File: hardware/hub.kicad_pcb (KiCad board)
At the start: 4 copper layers, 100 x 85 mm, 153 parts, among them J101 USB-A, J102 TNG-Power-BTM, J103 TNG-Power-TOP, J104 TNG-Data-BTM, J105 TNG-Data-TOP, P101 Debug, P102 PE, P202 PWR IN, SW101 BOOT, T201 744272251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

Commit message: fix resistor value, put usb tht connectors in paste layer
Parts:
- R208: value 27 -> 27k
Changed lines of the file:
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@@
     (mod_text_size 1 1)
     (mod_text_width 0.15)
-    (pad_size 1.1 3.8)
-    (pad_drill 0)
+    (pad_size 3.5 3.5)
+    (pad_drill 2.3)
     (pad_to_mask_clearance 0)
     (aux_axis_origin 57.45 50.95)
@@
       (effects (font (size 0.2 0.2) (thickness 0.05)))
     )
-    (fp_text value 27 (at 0.05 -0.375 180) (layer F.Fab)
+    (fp_text value 27k (at 0.05 -0.375 180) (layer F.Fab)
       (effects (font (size 0.2 0.2) (thickness 0.05)))
     )
@@
     (pad 4 smd rect (at 3.5 -4.2 270) (size 1.1 4) (layers F.Cu F.Paste F.Mask)
       (net 67 GND))
-    (pad "" thru_hole circle (at -6.57 0 270) (size 3.5 3.5) (drill 2.3) (layers *.Cu *.Mask))
-    (pad SHD thru_hole circle (at 6.57 0 270) (size 3.5 3.5) (drill 2.3) (layers *.Cu *.Mask F.SilkS)
+    (pad "" thru_hole circle (at -6.57 0 270) (size 3.5 3.5) (drill 2.3) (layers *.Cu *.Mask F.Paste))
+    (pad SHD thru_hole circle (at 6.57 0 270) (size 3.5 3.5) (drill 2.3) (layers *.Cu *.Mask F.Paste)
       (net 1 Earth))
     (model Connectors/USB_Type_B_Socket.wrl

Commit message: fix value
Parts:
- R114: value 510 -> 1k

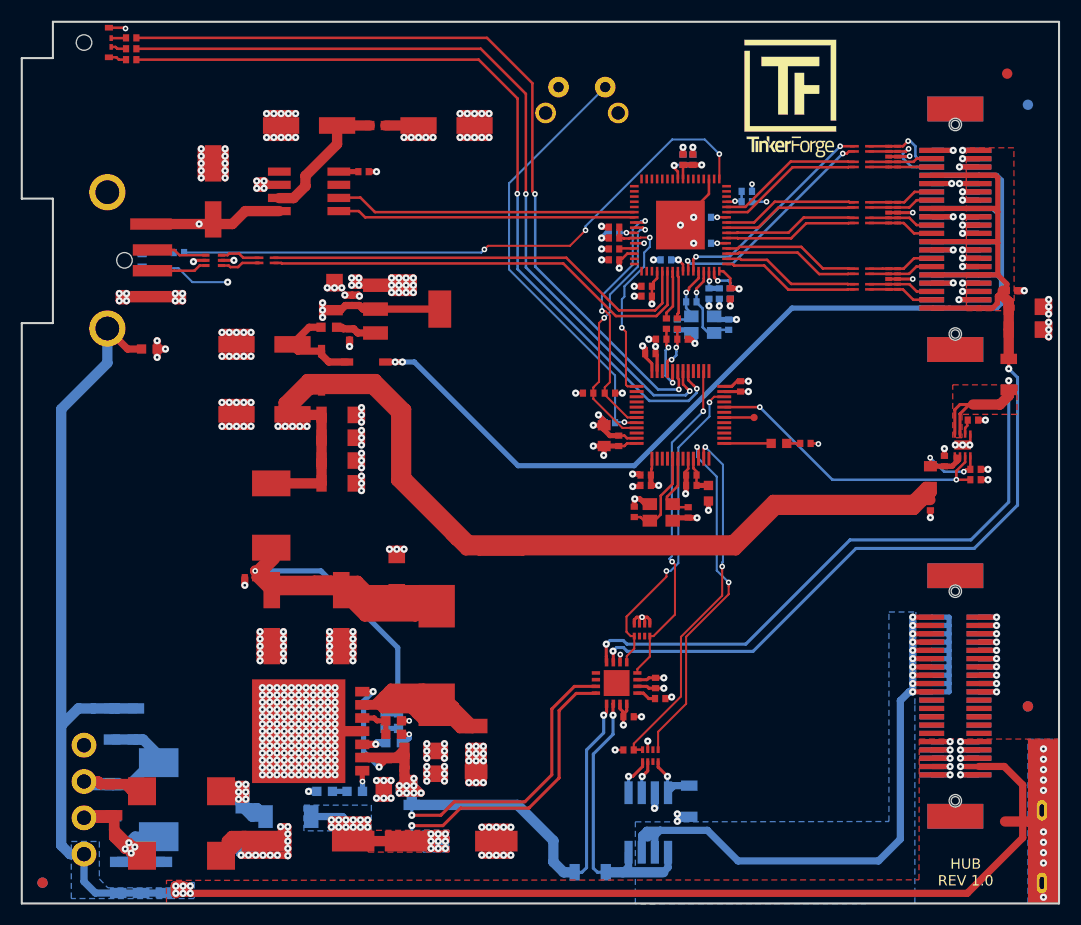
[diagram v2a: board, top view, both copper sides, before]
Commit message: add version 1.2
 * fix footprints
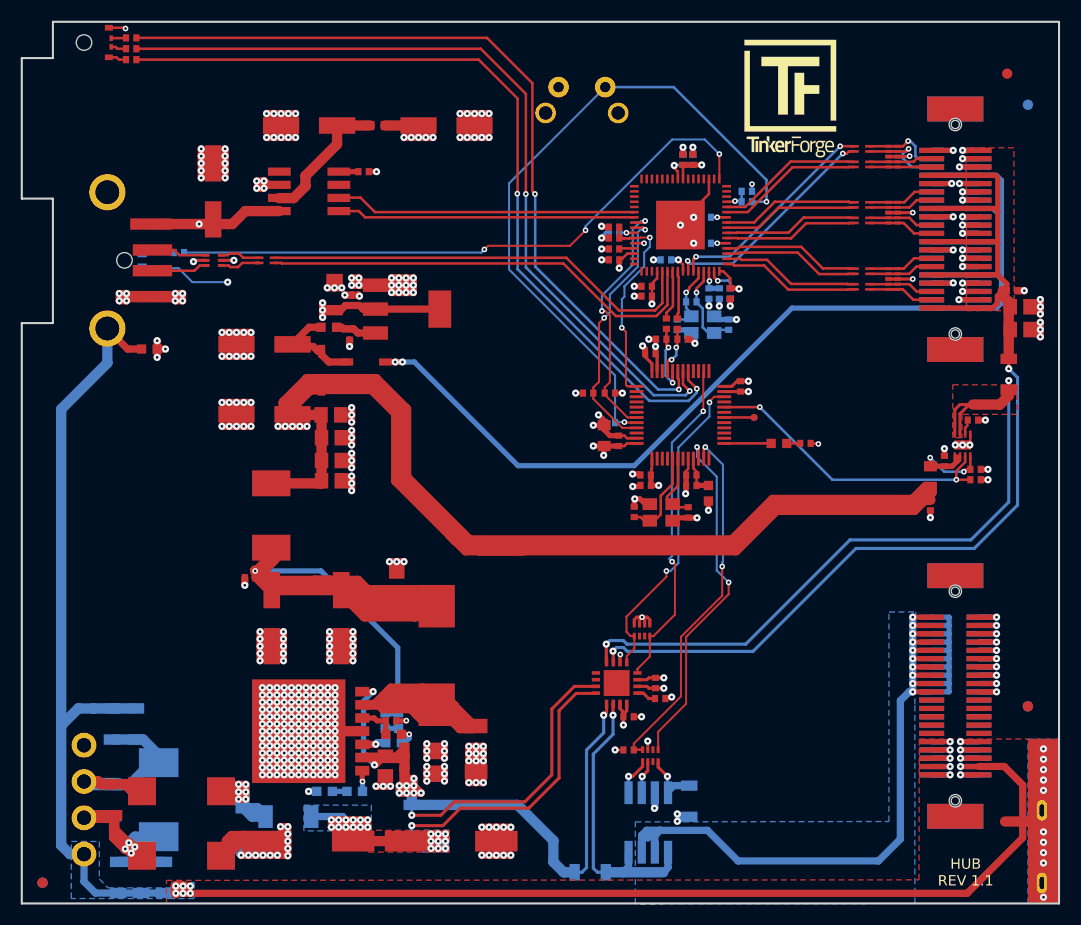
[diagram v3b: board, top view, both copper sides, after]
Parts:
- C108, C109, C117: value >100uF -> 100uF
- C135, C136, C215, C218, C223, C224, C225: footprint C1206 -> kicad-libraries:C0805E
- C137, C138: value TBD -> 12pF
- C201, C202: value 10uF -> 10uF/35V
- C205: value 100nF -> 100nF/35V; footprint C1206 -> kicad-libraries:C0805E
- C208: footprint C0603F -> kicad-libraries:C0402F
- C216, C219, C220: value >100µF -> 100µF
- R108: value 10k -> 1k
- R109: value DNP -> 10k
- T201: footprint kicad-libraries:WE-SL5 -> WE-SL5
- X102: value TBD -> 8MHz
- moved C215 0.80 mm to (93.6, 105.0)
- moved C205 0.76 mm to (92.5, 122.7)
- moved C218 0.60 mm to (87.3, 95.2)
- moved C223 0.60 mm to (87.2, 88.8)
- moved C224 0.55 mm to (87.3, 93.2)
- moved C225 0.55 mm to (87.3, 91.0)
- moved C135 0.40 mm to (153.7, 78.4)
- moved C136 0.40 mm to (153.7, 80.6)
- moved C208 0.25 mm to (93.0, 118.3)
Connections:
- net SW_24_STACK renamed SW_24_ENABLE
- net SW_5_STACK renamed SW_5_ENABLE
- J102 pad 21: (no net) -> Net-(J102-Pad21)
- J102 pad 22: (no net) -> Net-(J102-Pad22)
- J102 pad 23: (no net) -> Net-(J102-Pad23)
- J102 pad 24: (no net) -> Net-(J102-Pad24)
- J102 pad 25: (no net) -> Net-(J102-Pad25)
- J102 pad 26: (no net) -> Net-(J102-Pad26)
- J102 pad 27: (no net) -> Net-(J102-Pad27)
- J102 pad 28: (no net) -> Net-(J102-Pad28)
- J102 pad 29: (no net) -> Net-(J102-Pad29)
- J102 pad 30: (no net) -> Net-(J102-Pad30)
- J103 pad 21: (no net) -> Net-(J103-Pad21)
- J103 pad 22: (no net) -> Net-(J103-Pad22)
- J103 pad 23: (no net) -> Net-(J103-Pad23)
- J103 pad 24: (no net) -> Net-(J103-Pad24)
- J103 pad 25: (no net) -> Net-(J103-Pad25)
- J103 pad 26: (no net) -> Net-(J103-Pad26)
- J103 pad 27: (no net) -> Net-(J103-Pad27)
- J103 pad 28: (no net) -> Net-(J103-Pad28)
- J103 pad 29: (no net) -> Net-(J103-Pad29)
- J103 pad 30: (no net) -> Net-(J103-Pad30)
- J104 pad 12: (no net) -> Net-(J104-Pad12)
- J104 pad 14: (no net) -> Net-(J104-Pad14)
- J104 pad 20: (no net) -> Net-(J104-Pad20)
- J104 pad 22: (no net) -> Net-(J104-Pad22)
- J104 pad 28: (no net) -> Net-(J104-Pad28)
- J104 pad 30: (no net) -> Net-(J104-Pad30)
- J104 pad 36: (no net) -> Net-(J104-Pad36)
- J104 pad 38: (no net) -> Net-(J104-Pad38)
- P202 pad 1: (no net) -> Net-(P202-Pad1)
- R108 pad 2: 3V3 -> BOOT
- R114 pad 2: Net-(R114-Pad2) -> BOOT
- RP102 pad 3: (no net) -> Net-(RP102-Pad3)
- RP102 pad 6: (no net) -> Net-(RP102-Pad6)
- RP201 pad 6: (no net) -> Net-(RP201-Pad6)
- RP201 pad 7: (no net) -> Net-(RP201-Pad7)
- SW101 pad 2: Net-(R114-Pad2) -> BOOT
- U101 pad 14: (no net) -> Net-(U101-Pad14)
- U101 pad 15: (no net) -> Net-(U101-Pad15)
- U101 pad 16: (no net) -> Net-(U101-Pad16)
- U101 pad 18: (no net) -> Net-(U101-Pad18)
- U101 pad 20: (no net) -> Net-(U101-Pad20)
- U101 pad 21: (no net) -> Net-(U101-Pad21)
- U101 pad 22: (no net) -> Net-(U101-Pad22)
- U101 pad 23: (no net) -> Net-(U101-Pad23)
- U101 pad 26: (no net) -> Net-(U101-Pad26)
- U101 pad 27: (no net) -> Net-(U101-Pad27)
- U101 pad 28: (no net) -> Net-(U101-Pad28)
- U101 pad 29: (no net) -> Net-(U101-Pad29)
- U101 pad 30: (no net) -> Net-(U101-Pad30)
- U101 pad 31: (no net) -> Net-(U101-Pad31)
- U101 pad 32: (no net) -> Net-(U101-Pad32)
- U101 pad 33: (no net) -> Net-(U101-Pad33)
- U101 pad 34: (no net) -> Net-(U101-Pad34)
- U101 pad 35: (no net) -> Net-(U101-Pad35)
- U101 pad 36: (no net) -> Net-(U101-Pad36)
- U101 pad 37: (no net) -> Net-(U101-Pad37)
- U101 pad 47: (no net) -> Net-(U101-Pad47)
- U101 pad 48: (no net) -> Net-(U101-Pad48)
- U101 pad 49: (no net) -> Net-(U101-Pad49)
- U101 pad 50: (no net) -> Net-(U101-Pad50)
- U101 pad 51: (no net) -> Net-(U101-Pad51)
- U102 pad 3: (no net) -> Net-(U102-Pad3)
- U102 pad 5: (no net) -> Net-(U102-Pad5)
- U104 pad 12: (no net) -> Net-(U104-Pad12)
- U104 pad 14: (no net) -> Net-(U104-Pad14)
- U104 pad 15: (no net) -> Net-(U104-Pad15)
- U104 pad 16: (no net) -> Net-(U104-Pad16)
- U104 pad 17: (no net) -> Net-(U104-Pad17)
- U104 pad 19: (no net) -> Net-(U104-Pad19)
- U104 pad 2: (no net) -> Net-(U104-Pad2)
- U104 pad 21: (no net) -> Net-(U104-Pad21)
- U104 pad 25: (no net) -> Net-(U104-Pad25)
- U104 pad 27: (no net) -> Net-(U104-Pad27)
- U104 pad 28: (no net) -> Net-(U104-Pad28)
- U104 pad 3: (no net) -> Net-(U104-Pad3)
- U104 pad 34: (no net) -> Net-(U104-Pad34)
- U104 pad 38: (no net) -> Net-(U104-Pad38)
- U104 pad 39: (no net) -> Net-(U104-Pad39)
- U104 pad 4: (no net) -> Net-(U104-Pad4)
- U104 pad 40: (no net) -> Net-(U104-Pad40)
- U104 pad 41: (no net) -> Net-(U104-Pad41)
- U104 pad 42: (no net) -> Net-(U104-Pad42)
- U104 pad 44: Net-(R114-Pad2) -> BOOT
- U104 pad 46: (no net) -> Net-(U104-Pad46)
- U104 pad 7: (no net) -> Net-(U104-Pad7)
- U204 pad 10: (no net) -> Net-(U204-Pad10)
- U204 pad 9: (no net) -> Net-(U204-Pad9)
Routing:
- net BOOT: track 0.00 -> 65.3 mm, vias 0 -> 2
- net Net-(R114-Pad2): track 42.6 -> 0.00 mm, vias 1 -> 0
- net GND: track 859.2 -> 857.3 mm, vias 402 -> 399
- net 3V3: track 78.9 -> 77.5 mm, vias 32 -> 31
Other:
- board text added: "Copyright Tinkerforge GmbH 2020. This documentation describes Open Hardware and is licensed under the CERN OHL v. 1.1. You may redistribute and modify this documentation under the terms of the CERN OHL v.1.1. (http://ohwr.org/cernohl). This documentation is distributed WITHOUT ANY EXPRESS OR IMPLIED WARRANTY, INCLUDING OF MERCHANTABILITY, SATISFACTORY QUALITY AND FITNESS FOR A PARTICULAR PURPOSE.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"
- board text added: "HUB REV 1.1"
- board text removed: "HUB REV 1.0"

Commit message: fix values
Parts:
- C121, C122: value TBD/47pF -> 47pF
- C137, C138: value 12pF -> 33pF

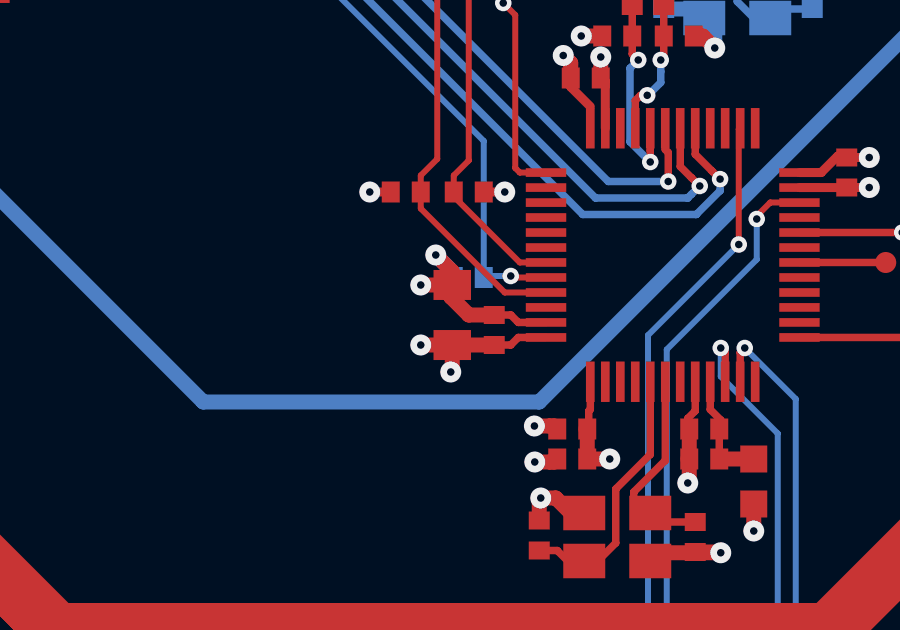
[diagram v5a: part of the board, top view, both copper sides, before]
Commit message: fix footprints
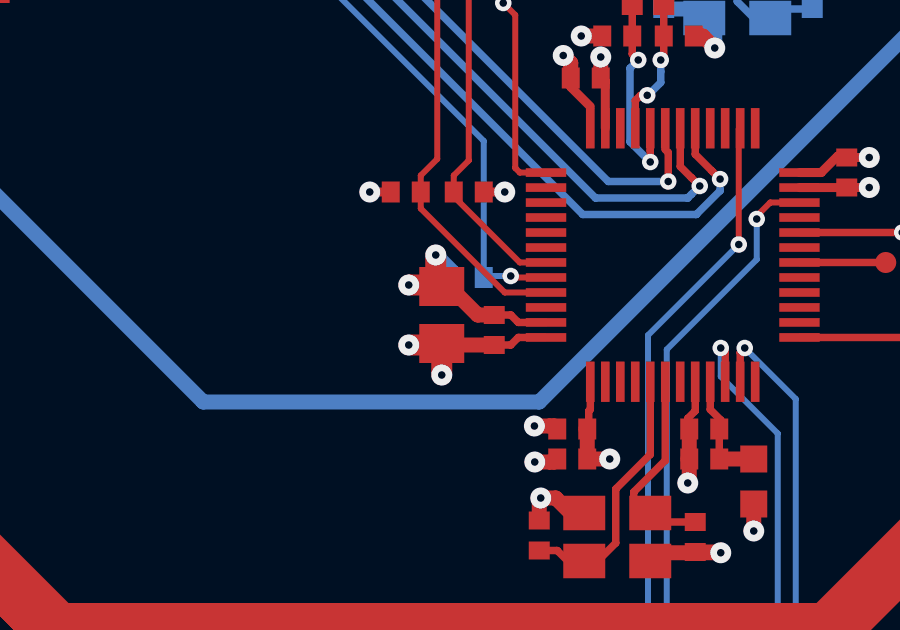
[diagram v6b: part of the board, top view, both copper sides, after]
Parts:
- C139: footprint C0805 -> kicad-libraries:C0805E
- C203: value TBD -> 100uF
- moved C139 0.35 mm to (113.2, 90.8)

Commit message: drc
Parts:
- R118: footprint kicad-libraries:1206 -> kicad-libraries:R1206
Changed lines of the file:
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@@
   )
   (setup
-    (last_trace_width 0.7)
+    (last_trace_width 0.15)
     (user_trace_width 0.15)
     (user_trace_width 0.2)
@@
     (add_net STACK_USB_D4_F-)
   )
+  (module kicad-libraries:USB-A-SMT-8231 (layer F.Cu)
+    (at 65.7 73.95 270)
+    (attr smd)
+    (fp_text reference J101 (at 0 1.7 90) (layer F.Fab)
+      (effects (font (size 0.59944 0.59944) (thickness 0.12446)))
+    )
+    (fp_text value USB-A (at 0 0 90) (layer F.Fab)
+      (effects (font (size 0.59944 0.59944) (thickness 0.12446)))
+    )
+    (fp_line (start -7.2 10.3) (end -7.2 -4.1) (layer F.Fab) (width 0.001))
+    (fp_line (start -7.2 -4.1) (end 7.2 -4.1) (layer F.Fab) (width 0.001))
+    (fp_line (start 7.2 -4.1) (end 7.2 10.3) (layer F.Fab) (width 0.001))
+    (fp_line (start 7.2 10.3) (end -7.2 10.3) (layer F.Fab) (width 0.001))
+    (fp_line (start 9 0) (end 9 20) (layer Dwgs.User) (width 0.1))
+    (fp_line (start -9 0) (end -9 20) (layer Dwgs.User) (width 0.1))
+    (pad 1 smd rect (at -3.5 -4.2 270) (size 1.1 4) (layers F.Cu F.Paste F.Mask)
+      (net 37 USB-PWR))
+    (pad 2 smd rect (at -1 -4.35 270) (size 1.1 3.8) (layers F.Cu F.Paste F.Mask)
+      (net 41 EXT_USB_D_F-))
+    (pad 3 smd rect (at 1 -4.35 270) (size 1.1 3.8) (layers F.Cu F.Paste F.Mask)
+      (net 42 EXT_USB_D_F+))
+    (pad 4 smd rect (at 3.5 -4.2 270) (size 1.1 4) (layers F.Cu F.Paste F.Mask)
+      (net 67 GND))
+    (pad "" thru_hole circle (at -6.57 0 270) (size 3.5 3.5) (drill 2.3) (layers *.Cu *.Mask F.Paste))
+    (pad SHD thru_hole circle (at 6.57 0 270) (size 3.5 3.5) (drill 2.3) (layers *.Cu *.Mask F.Paste)
+      (net 1 Earth))
+    (model Connectors/USB_Type_B_Socket.wrl
+      (offset (xyz 0 -3.428999948501587 0))
+      (scale (xyz 1 1 1))
+      (rotate (xyz 0 0 0))
+    )
+  )
   (module kicad-libraries:ELKO_103 (layer F.Cu)
     (at 98.85 129.9437 180)
@@
     )
   )
-  (module kicad-libraries:1206 (layer B.Cu)
-    (at 121.8 126.0937 90)
-    (attr smd)
-    (fp_text reference R118 (at 0 -0.5375 90) (layer B.Fab)
-      (effects (font (size 0.3 0.3) (thickness 0.075)) (justify mirror))
-    )
-    (fp_text value 1k (at 0 0.65 90) (layer B.Fab)
-      (effects (font (size 0.3 0.3) (thickness 0.075)) (justify mirror))
-    )
-    (fp_line (start -2.25044 1.09982) (end -2.25044 -1.09982) (layer B.Fab) (width 0.001))
-    (fp_line (start -2.25044 -1.09982) (end 2.25044 -1.09982) (layer B.Fab) (width 0.001))
-    (fp_line (start 2.25044 -1.09982) (end 2.25044 1.09982) (layer B.Fab) (width 0.001))
-    (fp_line (start 2.25044 1.09982) (end -2.25044 1.09982) (layer B.Fab) (width 0.001))
-    (pad 1 smd rect (at -1.50114 0 90) (size 1.00076 1.6002) (layers B.Cu B.Paste B.Mask)
-      (net 67 GND))
-    (pad 2 smd rect (at 1.50114 0 90) (size 1.00076 1.6002) (layers B.Cu B.Paste B.Mask)
-      (net 40 "Net-(R118-Pad2)"))
-  )
   (module kicad-libraries:Logo_TF_10x12 (layer F.Cu)
     (at 131.55 58.2)
@@
     )
   )
-  (module kicad-libraries:USB-A-SMT-8231 (layer F.Cu)
-    (at 65.7 73.95 270)
-    (attr smd)
-    (fp_text reference J101 (at 0 1.7 90) (layer F.Fab)
-      (effects (font (size 0.59944 0.59944) (thickness 0.12446)))
-    )
-    (fp_text value USB-A (at 0 0 90) (layer F.Fab)
-      (effects (font (size 0.59944 0.59944) (thickness 0.12446)))
-    )
-    (fp_line (start -7.2 10.3) (end -7.2 -4.1) (layer F.Fab) (width 0.001))
-    (fp_line (start -7.2 -4.1) (end 7.2 -4.1) (layer F.Fab) (width 0.001))
-    (fp_line (start 7.2 -4.1) (end 7.2 10.3) (layer F.Fab) (width 0.001))
-    (fp_line (start 7.2 10.3) (end -7.2 10.3) (layer F.Fab) (width 0.001))
-    (fp_line (start 9 0) (end 9 20) (layer Dwgs.User) (width 0.1))
-    (fp_line (start -9 0) (end -9 20) (layer Dwgs.User) (width 0.1))
-    (pad 1 smd rect (at -3.5 -4.2 270) (size 1.1 4) (layers F.Cu F.Paste F.Mask)
-      (net 37 USB-PWR))
-    (pad 2 smd rect (at -1 -4.35 270) (size 1.1 3.8) (layers F.Cu F.Paste F.Mask)
-      (net 41 EXT_USB_D_F-))
-    (pad 3 smd rect (at 1 -4.35 270) (size 1.1 3.8) (layers F.Cu F.Paste F.Mask)
-      (net 42 EXT_USB_D_F+))
-    (pad 4 smd rect (at 3.5 -4.2 270) (size 1.1 4) (layers F.Cu F.Paste F.Mask)
-      (net 67 GND))
-    (pad "" thru_hole circle (at -6.57 0 270) (size 3.5 3.5) (drill 2.3) (layers *.Cu *.Mask F.Paste))
-    (pad SHD thru_hole circle (at 6.57 0 270) (size 3.5 3.5) (drill 2.3) (layers *.Cu *.Mask F.Paste)
-      (net 1 Earth))
-    (model Connectors/USB_Type_B_Socket.wrl
-      (offset (xyz 0 -3.428999948501587 0))
-      (scale (xyz 1 1 1))
-      (rotate (xyz 0 0 0))
-    )
-  )
   (module TNG-40-BTM (layer B.Cu)
     (at 147.45 115.95 270)
@@
       (at (xyz 0 0 0))
       (scale (xyz 1 1 1))
+      (rotate (xyz 0 0 0))
+    )
+  )
+  (module kicad-libraries:R1206 (layer B.Cu)
+    (at 121.8 126.0937 90)
+    (attr smd)
+    (fp_text reference R118 (at 0 -0.5375 90) (layer B.Fab)
+      (effects (font (size 0.3 0.3) (thickness 0.075)) (justify mirror))
+    )
+    (fp_text value 1k (at 0 0.65 90) (layer B.Fab)
+      (effects (font (size 0.3 0.3) (thickness 0.075)) (justify mirror))
+    )
+    (fp_line (start -2.25044 1.09982) (end -2.25044 -1.09982) (layer B.Fab) (width 0.001))
+    (fp_line (start -2.25044 -1.09982) (end 2.25044 -1.09982) (layer B.Fab) (width 0.001))
+    (fp_line (start 2.25044 -1.09982) (end 2.25044 1.09982) (layer B.Fab) (width 0.001))
+    (fp_line (start 2.25044 1.09982) (end -2.25044 1.09982) (layer B.Fab) (width 0.001))
+    (pad 1 smd rect (at -1.50114 0 90) (size 1.00076 1.6002) (layers B.Cu B.Paste B.Mask)
+      (net 67 GND))
+    (pad 2 smd rect (at 1.50114 0 90) (size 1.00076 1.6002) (layers B.Cu B.Paste B.Mask)
+      (net 40 "Net-(R118-Pad2)"))
+    (model Resistors_SMD/R_1206.wrl
+      (at (xyz 0 0 0))
+      (scale (xyz 1 1 1))

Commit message: fix values
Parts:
- C128: value 1µF -> 1uF
- C216, C219, C220: value 100µF -> 100uF
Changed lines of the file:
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@@
       (effects (font (size 0.59944 0.59944) (thickness 0.12446)))
     )
-    (fp_text value 100µF (at 0.95 -0.375 90) (layer F.Fab)
+    (fp_text value 100uF (at 0.95 -0.375 90) (layer F.Fab)
       (effects (font (size 0.59944 0.59944) (thickness 0.12446)))
     )
@@
       (effects (font (size 0.59944 0.59944) (thickness 0.12446)))
     )
-    (fp_text value 100µF (at 0.95 -0.375 90) (layer F.Fab)
+    (fp_text value 100uF (at 0.95 -0.375 90) (layer F.Fab)
       (effects (font (size 0.59944 0.59944) (thickness 0.12446)))
     )
@@
       (effects (font (size 0.2 0.2) (thickness 0.05)))
     )
-    (fp_text value 1µF (at 0 -0.15) (layer F.Fab)
+    (fp_text value 1uF (at 0 -0.15) (layer F.Fab)
       (effects (font (size 0.2 0.2) (thickness 0.05)))
     )
@@
       (effects (font (size 0.59944 0.59944) (thickness 0.12446)))
     )
-    (fp_text value 100µF (at 0.95 -0.375) (layer F.Fab)
+    (fp_text value 100uF (at 0.95 -0.375) (layer F.Fab)
       (effects (font (size 0.59944 0.59944) (thickness 0.12446)))
     )
